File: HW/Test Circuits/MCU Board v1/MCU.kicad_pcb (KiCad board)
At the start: 2 copper layers, 62.2 x 33 mm, 5 parts, among them J1 IN, J2 OUT

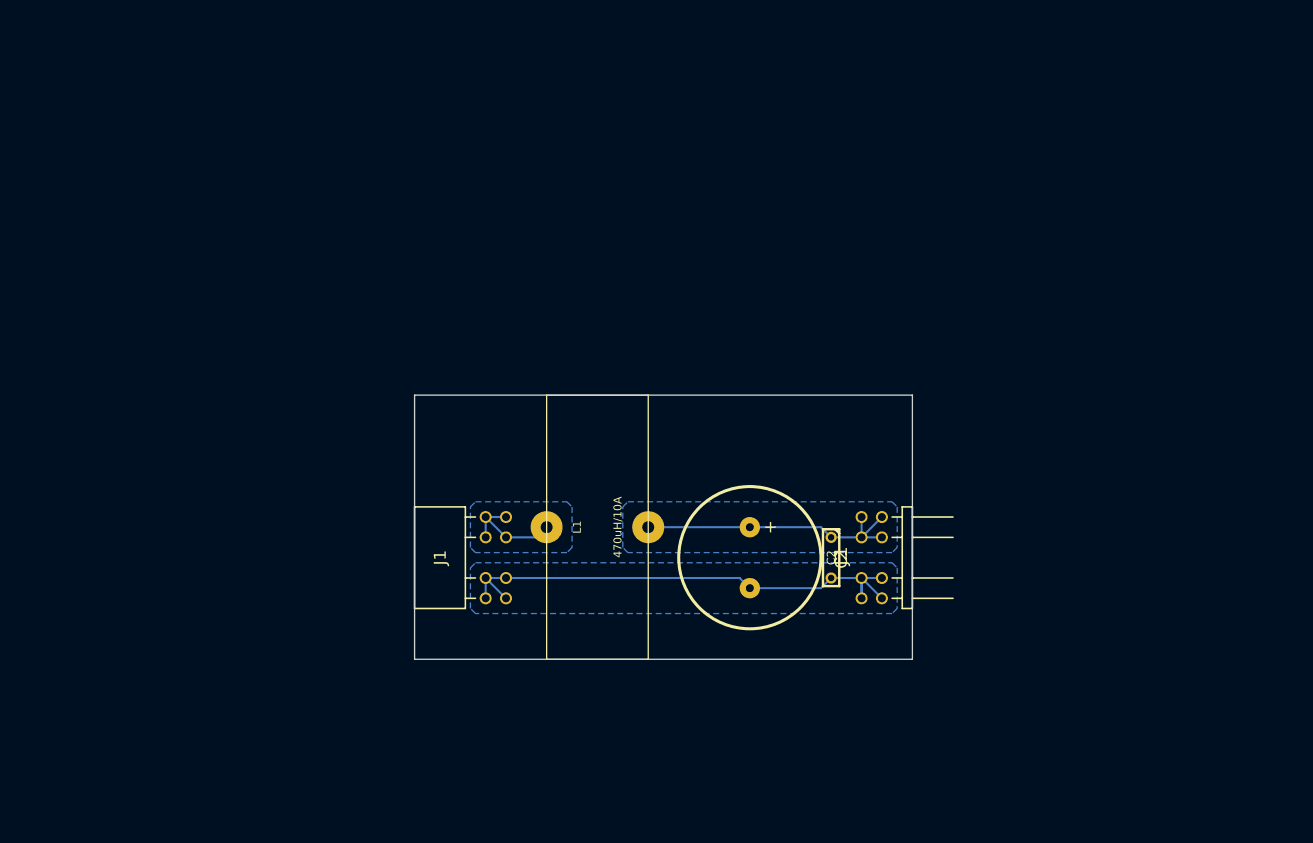
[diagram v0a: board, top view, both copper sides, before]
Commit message: MCU Board v1 updated +cleanup DO NOT BUILD IT, BUGGY !!!
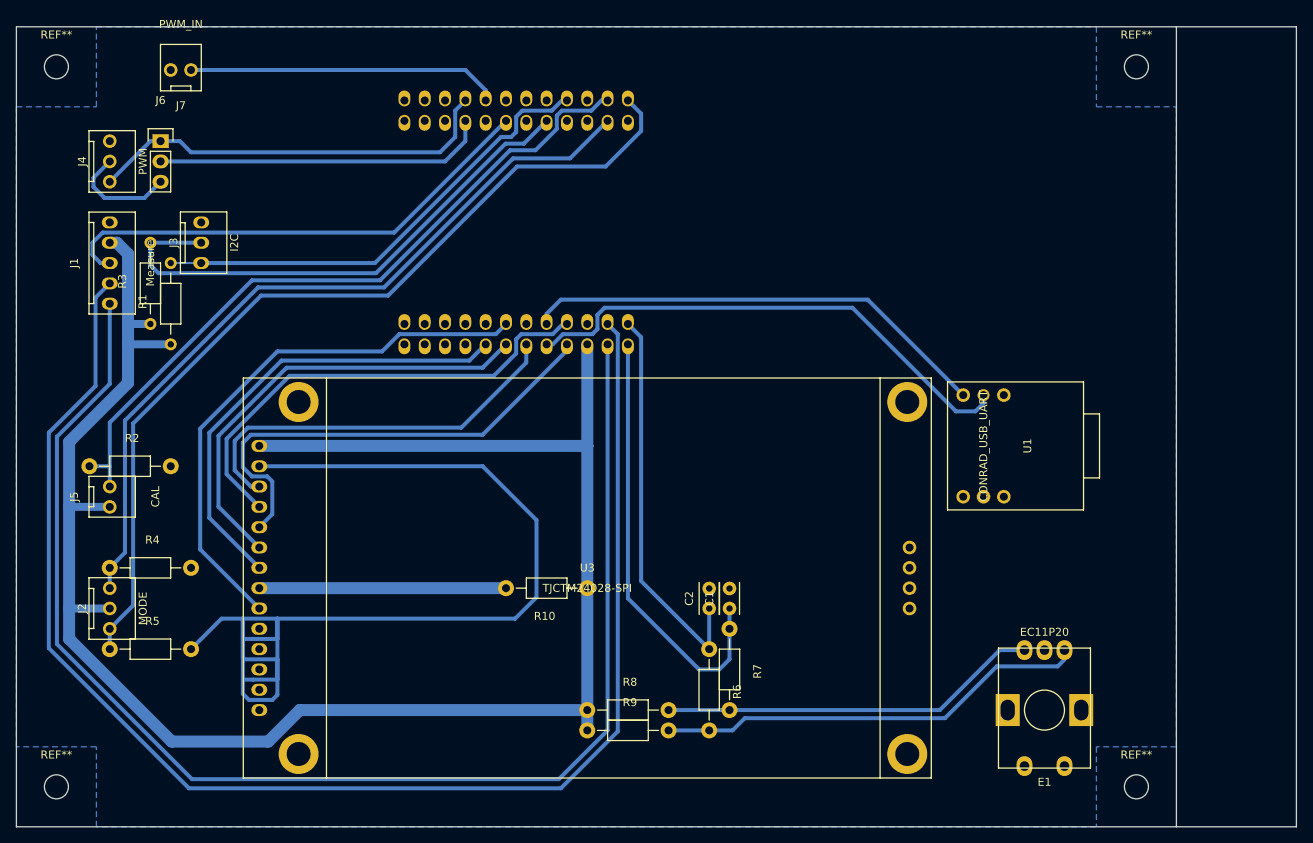
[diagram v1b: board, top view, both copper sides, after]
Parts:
- removed L1: 470uH/10A, L-TOROID-D35X5
- added E1: EC11P20, suf_switch:EC11P20_single_side, F.Cu at (143.5, 105.4)
- added J3: I2C, suf_connector_ncw:CONN_NCW254-03S, F.Cu at (38.1, 47.0)
- added J4: PWM, suf_connector_ncw:CONN_NCW254-03S, F.Cu at (26.7, 36.8)
- added J5: CAL, suf_connector_ncw:CONN_NCW254-02S, F.Cu at (26.7, 78.7)
- added J6: PWM_DUAL, Pin_Headers:Pin_Header_Straight_1x03, F.Cu at (33.0, 34.3)
- added J7: PWM_IN, suf_connector_ncw:CONN_NCW254-02S, F.Cu at (35.6, 25.4)
- added R1: 10K, Resistors_ThroughHole:Resistor_Horizontal_RM10mm, F.Cu at (34.3, 54.6)
- added R10: 3R9, Resistors_ThroughHole:Resistor_Horizontal_RM10mm, F.Cu at (81.3, 90.2)
- added R2: 47K, Resistors_ThroughHole:Resistor_Horizontal_RM10mm, F.Cu at (29.2, 74.9)
- added R3: 10K, Resistors_ThroughHole:Resistor_Horizontal_RM10mm, F.Cu at (31.8, 52.1)
- added R4: 47K, Resistors_ThroughHole:Resistor_Horizontal_RM10mm, F.Cu at (31.8, 87.6)
- added R5: 47K, Resistors_ThroughHole:Resistor_Horizontal_RM10mm, F.Cu at (31.8, 97.8)
- added R6: 10K, Resistors_ThroughHole:Resistor_Horizontal_RM10mm, F.Cu at (101.6, 102.9)
- added R7: 10K, Resistors_ThroughHole:Resistor_Horizontal_RM10mm, F.Cu at (104.1, 100.3)
- added R8: 10K, Resistors_ThroughHole:Resistor_Horizontal_RM10mm, F.Cu at (91.4, 105.4)
- added R9: 10K, Resistors_ThroughHole:Resistor_Horizontal_RM10mm, F.Cu at (91.4, 108.0)
- added REF**: MountingHole_3mm, Mounting_Holes:MountingHole_3mm, F.Cu at (20.0, 25.0)
- added REF**: MountingHole_3mm, Mounting_Holes:MountingHole_3mm, F.Cu at (20.0, 115.0)
- added REF**: MountingHole_3mm, Mounting_Holes:MountingHole_3mm, F.Cu at (155.0, 25.0)
- added REF**: MountingHole_3mm, Mounting_Holes:MountingHole_3mm, F.Cu at (155.0, 115.0)
- added U1: CONRAD_USB_UART, suf_module:CONRAD_USB_UART, F.Cu at (135.9, 72.4)
- added U2: M0516LDN, suf_module:M0516-DEV, B.Cu at (77.5, 44.5)
- added U3: TJCTM24028-SPI, suf_display:TJCTM24028-SPI, F.Cu at (86.4, 88.9)
- C1: value 1000uF/63V -> 10nF; footprint C3P_D7 -> Capacitors_ThroughHole:C_Rect_L4_W2.5_P2.5
- C2: value 10nF/100V -> 10nF; footprint C2 -> Capacitors_ThroughHole:C_Rect_L4_W2.5_P2.5
- J1: value IN -> Measure; footprint MD-TEST-HDR-F -> suf_connector_ncw:CONN_NCW254-05S
- J2: value OUT -> MODE; footprint MD-TEST-HDR-M -> suf_connector_ncw:CONN_NCW254-03S
- moved J2 95.5 mm to (26.7, 92.7)
- moved J1 60.7 mm to (26.7, 49.5)
- moved C2 16.5 mm to (101.6, 92.7), turned to 90 degrees
- moved C1 6.84 mm to (104.1, 92.7), turned to 90 degrees
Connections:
- C1 pad 1: N-000003 -> ENC_B
- C2 pad 1: N-000003 -> ENC_A
- J1 pad 1: GND -> ADC_U
- J1 pad 2: GND -> ADC_I
- J1 pad 3: GND -> RPM_IN
- J1 pad 4: GND -> VCC
- J2 pad 1: GND -> MODE_RPM
- J2 pad 2: GND -> VCC
- J2 pad 3: GND -> MODE_AUTO
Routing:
- net VCC: track 0.00 -> 234.5 mm
- net ADC_I: track 0.00 -> 183.3 mm
- net ADC_U: track 0.00 -> 171.9 mm
- net MODE_RPM: track 0.00 -> 112.5 mm
- net MODE_AUTO: track 0.00 -> 97.6 mm
- net CAL: track 0.00 -> 90.4 mm
- net GND: track 65.4 -> 139.8 mm
- net TFT_MISO: track 0.00 -> 69.2 mm
- net I2C_SCL: track 0.00 -> 67.0 mm
- net RXD: track 0.00 -> 64.3 mm
- net RPM_IN: track 0.00 -> 62.1 mm
- net TFT_DC: track 0.00 -> 59.9 mm
- net TFT_RST: track 0.00 -> 59.7 mm
- net I2C_SDA: track 0.00 -> 59.7 mm
- net TXD: track 0.00 -> 59.0 mm
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- removed copper zone on B.Cu, net N-000002
- removed copper zone on B.Cu, net N-000003
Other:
- board size 62.2 x 33 mm -> 160 x 100 mm
